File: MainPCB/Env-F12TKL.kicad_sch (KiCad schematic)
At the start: 223 parts, among them J1 TSA343G00-250J2, U1 SOT-23-5 5.5V 3.3V 500mA, U2 RP2040, Y1 3225_4P

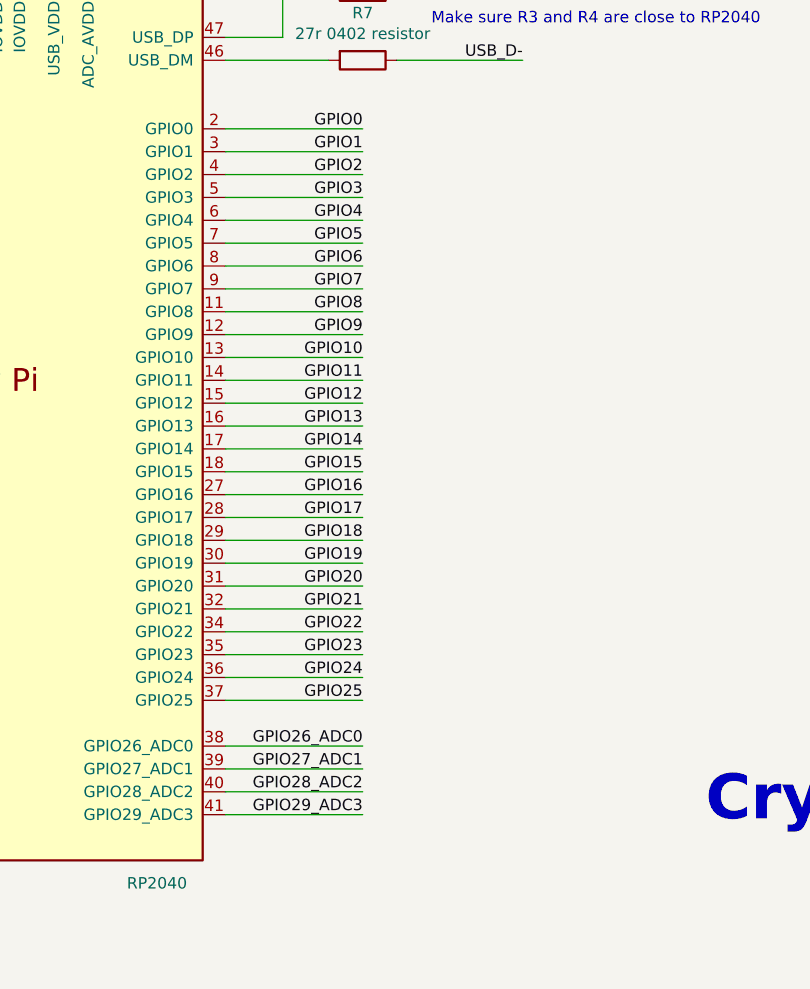
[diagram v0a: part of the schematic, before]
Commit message: wired up a whole bunch of matrix traces, now just need to add some I2C headers and some RGB connectors and some hidden cats among other illicit things like memes.
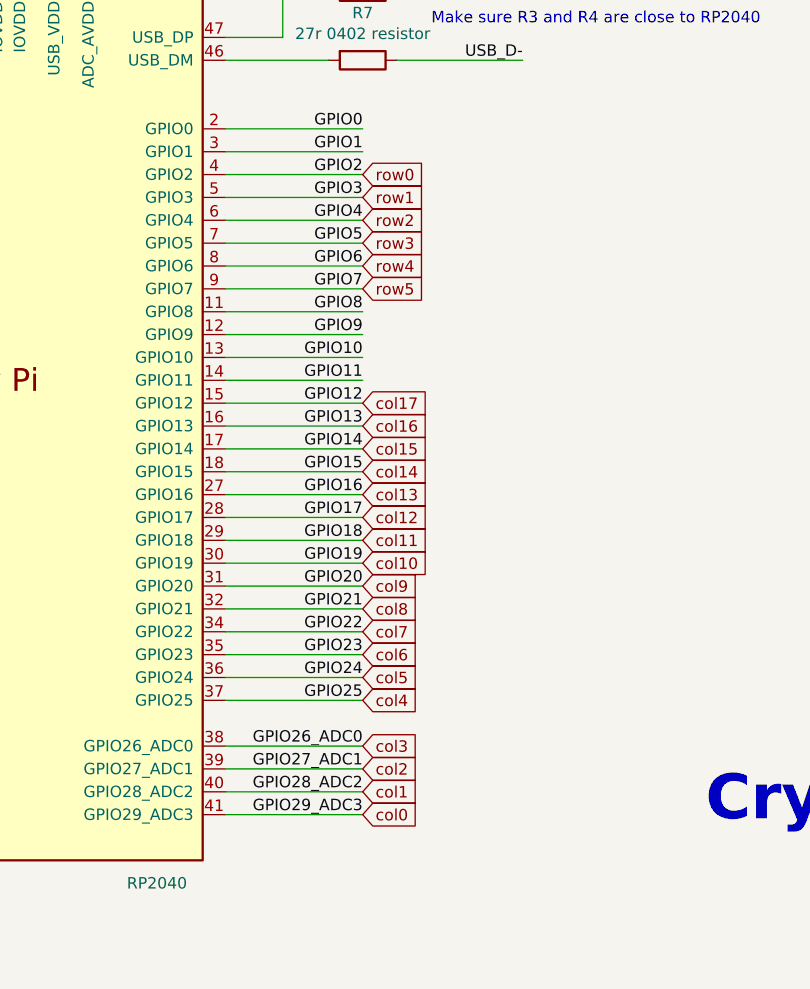
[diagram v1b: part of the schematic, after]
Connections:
- net GPIO12 is gone; now on net col17: U2.15 (GPIO12)
- net GPIO13 is gone; now on net col16: U2.16 (GPIO13)
- net GPIO14 is gone; now on net col15: U2.17 (GPIO14)
- net GPIO15 is gone; now on net col14: U2.18 (GPIO15)
- net GPIO16 is gone; now on net col13: U2.27 (GPIO16)
- net GPIO17 is gone; now on net col12: U2.28 (GPIO17)
- net GPIO18 is gone; now on net col11: U2.29 (GPIO18)
- net GPIO19 is gone; now on net col10: U2.30 (GPIO19)
- net GPIO2 is gone; now on net row0: U2.4 (GPIO2)
- net GPIO20 is gone; now on net col9: U2.31 (GPIO20)
- net GPIO21 is gone; now on net col8: U2.32 (GPIO21)
- net GPIO22 is gone; now on net col7: U2.34 (GPIO22)
- net GPIO23 is gone; now on net col6: U2.35 (GPIO23)
- net GPIO24 is gone; now on net col5: U2.36 (GPIO24)
- net GPIO25 is gone; now on net col4: U2.37 (GPIO25)
- net GPIO26_ADC0 is gone; now on net col3: U2.38 (GPIO26_ADC0)
- net GPIO27_ADC1 is gone; now on net col2: U2.39 (GPIO27_ADC1)
- net GPIO28_ADC2 is gone; now on net col1: U2.40 (GPIO28_ADC2)
- net GPIO29_ADC3 is gone; now on net col0: U2.41 (GPIO29_ADC3)
- net GPIO3 is gone; now on net row1: U2.5 (GPIO3)
- net GPIO4 is gone; now on net row2: U2.6 (GPIO4)
- net GPIO5 is gone; now on net row3: U2.7 (GPIO5)
- net GPIO6 is gone; now on net row4: U2.8 (GPIO6)
- net GPIO7 is gone; now on net row5: U2.9 (GPIO7)
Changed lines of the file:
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@@
     (effects (font (size 1.27 1.27)) (justify right bottom))
   )
+  (global_label "col0" (shape input) (at 299.72 375.92 0) (fields_autoplaced)
+    (effects (font (size 1.27 1.27)) (justify left))
+    (property "Intersheet References" "${INTERSHEET_REFS}" (id 0) (at 306.436 375.8406 0)
+      (effects (font (size 1.27 1.27)) (justify left) hide)
+    )
+  )
   (global_label "row0" (shape input) (at 31.75 43.18 180) (fields_autoplaced)
     (effects (font (size 1.27 1.27)) (justify right))
@@
     (property "Intersheet References" "${INTERSHEET_REFS}" (id 0) (at 3.81 7.62 0)
       (effects (font (size 1.27 1.27)) hide)
+    )
+  )
+  (global_label "col7" (shape input) (at 299.72 355.6 0) (fields_autoplaced)
+    (effects (font (size 1.27 1.27)) (justify left))
+    (property "Intersheet References" "${INTERSHEET_REFS}" (id 0) (at 306.436 355.5206 0)
+      (effects (font (size 1.27 1.27)) (justify left) hide)
     )
   )
@@
     )
   )
+  (global_label "col14" (shape input) (at 299.72 337.82 0) (fields_autoplaced)
+    (effects (font (size 1.27 1.27)) (justify left))
+    (property "Intersheet References" "${INTERSHEET_REFS}" (id 0) (at 306.436 337.7406 0)
+      (effects (font (size 1.27 1.27)) (justify left) hide)
+    )
+  )
   (global_label "col14" (shape input) (at 405.13 24.13 180) (fields_autoplaced)
     (effects (font (size 1.27 1.27)) (justify right))
@@
     (property "Intersheet References" "${INTERSHEET_REFS}" (id 0) (at 3.81 7.62 0)
       (effects (font (size 1.27 1.27)) hide)
+    )
+  )
+  (global_label "row4" (shape input) (at 299.72 314.96 0) (fields_autoplaced)
+    (effects (font (size 1.27 1.27)) (justify left))
+    (property "Intersheet References" "${INTERSHEET_REFS}" (id 0) (at 306.7988 314.8806 0)
+      (effects (font (size 1.27 1.27)) (justify left) hide)
+    )
+  )
+  (global_label "col17" (shape input) (at 299.72 330.2 0) (fields_autoplaced)
+    (effects (font (size 1.27 1.27)) (justify left))
+    (property "Intersheet References" "${INTERSHEET_REFS}" (id 0) (at 306.436 330.1206 0)
+      (effects (font (size 1.27 1.27)) (justify left) hide)
     )
   )
@@
     )
   )
+  (global_label "col6" (shape input) (at 299.72 358.14 0) (fields_autoplaced)
+    (effects (font (size 1.27 1.27)) (justify left))
+    (property "Intersheet References" "${INTERSHEET_REFS}" (id 0) (at 306.436 358.0606 0)
+      (effects (font (size 1.27 1.27)) (justify left) hide)
+    )
+  )
+  (global_label "col2" (shape input) (at 299.72 370.84 0) (fields_autoplaced)
+    (effects (font (size 1.27 1.27)) (justify left))
+    (property "Intersheet References" "${INTERSHEET_REFS}" (id 0) (at 306.436 370.7606 0)
+      (effects (font (size 1.27 1.27)) (justify left) hide)
+    )
+  )
+  (global_label "col9" (shape input) (at 299.72 350.52 0) (fields_autoplaced)
+    (effects (font (size 1.27 1.27)) (justify left))
+    (property "Intersheet References" "${INTERSHEET_REFS}" (id 0) (at 306.436 350.4406 0)
+      (effects (font (size 1.27 1.27)) (justify left) hide)
+    )
+  )
+  (global_label "col10" (shape input) (at 299.72 347.98 0) (fields_autoplaced)
+    (effects (font (size 1.27 1.27)) (justify left))
+    (property "Intersheet References" "${INTERSHEET_REFS}" (id 0) (at 306.436 347.9006 0)
+      (effects (font (size 1.27 1.27)) (justify left) hide)
+    )
+  )
   (global_label "col17" (shape input) (at 481.33 24.13 180) (fields_autoplaced)
     (effects (font (size 1.27 1.27)) (justify right))
@@
     (property "Intersheet References" "${INTERSHEET_REFS}" (id 0) (at 3.81 7.62 0)
       (effects (font (size 1.27 1.27)) hide)
+    )
+  )
+  (global_label "col4" (shape input) (at 299.72 363.22 0) (fields_autoplaced)
+    (effects (font (size 1.27 1.27)) (justify left))
+    (property "Intersheet References" "${INTERSHEET_REFS}" (id 0) (at 306.436 363.1406 0)
+      (effects (font (size 1.27 1.27)) (justify left) hide)
+    )
+  )
+  (global_label "col15" (shape input) (at 299.72 335.28 0) (fields_autoplaced)
+    (effects (font (size 1.27 1.27)) (justify left))
+    (property "Intersheet References" "${INTERSHEET_REFS}" (id 0) (at 306.436 335.2006 0)
+      (effects (font (size 1.27 1.27)) (justify left) hide)
     )
   )
@@
     )
   )
+  (global_label "col3" (shape input) (at 299.72 368.3 0) (fields_autoplaced)
+    (effects (font (size 1.27 1.27)) (justify left))
+    (property "Intersheet References" "${INTERSHEET_REFS}" (id 0) (at 306.436 368.2206 0)
+      (effects (font (size 1.27 1.27)) (justify left) hide)
+    )
+  )
   (global_label "col9" (shape input) (at 278.13 24.13 180) (fields_autoplaced)
     (effects (font (size 1.27 1.27)) (justify right))
@@
     )
   )
+  (global_label "row0" (shape input) (at 299.72 304.8 0) (fields_autoplaced)
+    (effects (font (size 1.27 1.27)) (justify left))
+    (property "Intersheet References" "${INTERSHEET_REFS}" (id 0) (at 322.58 340.36 0)
+      (effects (font (size 1.27 1.27)) hide)
+    )
+  )
+  (global_label "row3" (shape input) (at 299.72 312.42 0) (fields_autoplaced)
+    (effects (font (size 1.27 1.27)) (justify left))
+    (property "Intersheet References" "${INTERSHEET_REFS}" (id 0) (at 306.7988 312.3406 0)
+      (effects (font (size 1.27 1.27)) (justify left) hide)
+    )
+  )
   (global_label "col15" (shape input) (at 430.53 24.13 180) (fields_autoplaced)
     (effects (font (size 1.27 1.27)) (justify right))
@@
     )
   )
+  (global_label "col5" (shape input) (at 299.72 360.68 0) (fields_autoplaced)
+    (effects (font (size 1.27 1.27)) (justify left))
+    (property "Intersheet References" "${INTERSHEET_REFS}" (id 0) (at 306.436 360.6006 0)
+      (effects (font (size 1.27 1.27)) (justify left) hide)
+    )
+  )
+  (global_label "row1" (shape input) (at 299.72 307.34 0) (fields_autoplaced)
+    (effects (font (size 1.27 1.27)) (justify left))
+    (property "Intersheet References" "${INTERSHEET_REFS}" (id 0) (at 306.7988 307.2606 0)
+      (effects (font (size 1.27 1.27)) (justify left) hide)
+    )
+  )
+  (global_label "col11" (shape input) (at 299.72 345.44 0) (fields_autoplaced)
+    (effects (font (size 1.27 1.27)) (justify left))
+    (property "Intersheet References" "${INTERSHEET_REFS}" (id 0) (at 306.436 345.3606 0)
+      (effects (font (size 1.27 1.27)) (justify left) hide)
+    )
+  )
   (global_label "col1" (shape input) (at 74.93 24.13 180) (fields_autoplaced)
     (effects (font (size 1.27 1.27)) (justify right))
@@
     )
   )
+  (global_label "row2" (shape input) (at 299.72 309.88 0) (fields_autoplaced)
+    (effects (font (size 1.27 1.27)) (justify left))
+    (property "Intersheet References" "${INTERSHEET_REFS}" (id 0) (at 306.7988 309.8006 0)
+      (effects (font (size 1.27 1.27)) (justify left) hide)
+    )
+  )
   (global_label "row3" (shape input) (at 31.75 119.38 180) (fields_autoplaced)
     (effects (font (size 1.27 1.27)) (justify right))
@@
     )
   )
+  (global_label "col16" (shape input) (at 299.72 332.74 0) (fields_autoplaced)
+    (effects (font (size 1.27 1.27)) (justify left))
+    (property "Intersheet References" "${INTERSHEET_REFS}" (id 0) (at 306.436 332.6606 0)
+      (effects (font (size 1.27 1.27)) (justify left) hide)
+    )
+  )
   (global_label "XOUT" (shape input) (at 219.71 340.36 180) (fields_autoplaced)
     (effects (font (size 1.27 1.27)) (justify right))
@@
     )
   )
+  (global_label "col12" (shape input) (at 299.72 342.9 0) (fields_autoplaced)
+    (effects (font (size 1.27 1.27)) (justify left))
+    (property "Intersheet References" "${INTERSHEET_REFS}" (id 0) (at 306.436 342.8206 0)
+      (effects (font (size 1.27 1.27)) (justify left) hide)
+    )
+  )
   (global_label "col0" (shape input) (at 49.53 24.13 180) (fields_autoplaced)
     (effects (font (size 1.27 1.27)) (justify right))
@@
     )
   )
+  (global_label "col8" (shape input) (at 299.72 353.06 0) (fields_autoplaced)
+    (effects (font (size 1.27 1.27)) (justify left))
+    (property "Intersheet References" "${INTERSHEET_REFS}" (id 0) (at 306.436 352.9806 0)
+      (effects (font (size 1.27 1.27)) (justify left) hide)
+    )
+  )
+  (global_label "row5" (shape input) (at 299.72 317.5 0) (fields_autoplaced)
+    (effects (font (size 1.27 1.27)) (justify left))
+    (property "Intersheet References" "${INTERSHEET_REFS}" (id 0) (at 306.7988 317.4206 0)
+      (effects (font (size 1.27 1.27)) (justify left) hide)
+    )
+  )
+  (global_label "col13" (shape input) (at 299.72 340.36 0) (fields_autoplaced)
+    (effects (font (size 1.27 1.27)) (justify left))
+    (property "Intersheet References" "${INTERSHEET_REFS}" (id 0) (at 306.436 340.2806 0)
+      (effects (font (size 1.27 1.27)) (justify left) hide)
+    )
+  )
+  (global_label "col1" (shape input) (at 299.72 373.38 0) (fields_autoplaced)
+    (effects (font (size 1.27 1.27)) (justify left))
+    (property "Intersheet References" "${INTERSHEET_REFS}" (id 0) (at 306.436 373.3006 0)
+      (effects (font (size 1.27 1.27)) (justify left) hide)
+    )
+  )

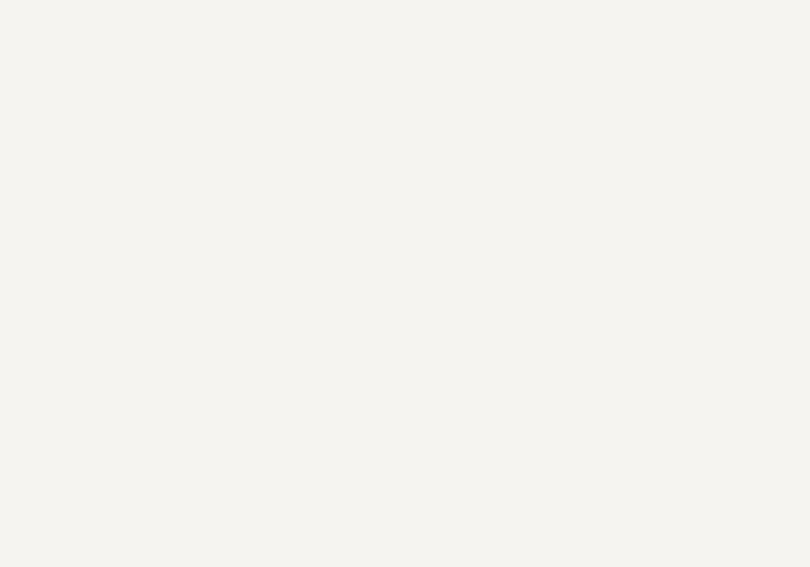
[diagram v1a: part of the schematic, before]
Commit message: added a GPIO breakout
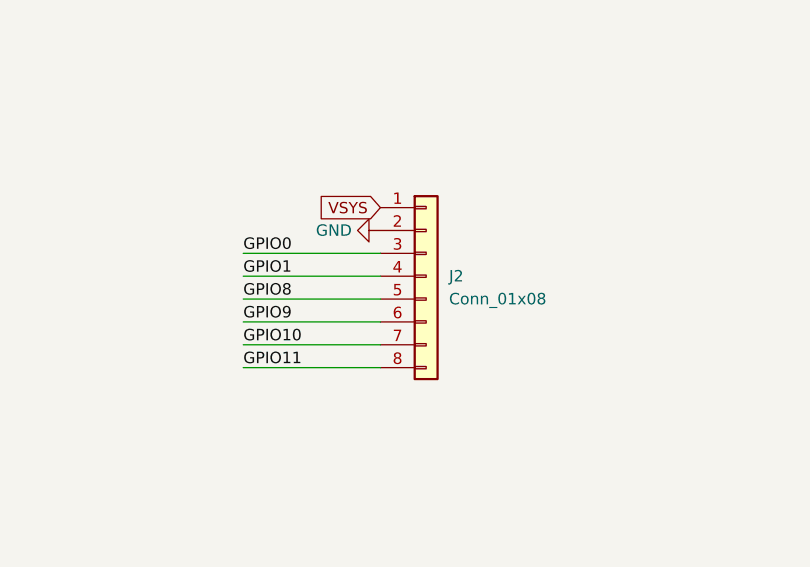
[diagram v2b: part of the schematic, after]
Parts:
- added J2: Conn_01x08, Connector_PinHeader_2.54mm:PinHeader_1x08_P2.54mm_Vertical, symbol Connector_Generic:Conn_01x08
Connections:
- net GND: now also J2.2 (Pin_2)
- net GPIO0: now also J2.3 (Pin_3)
- net GPIO1: now also J2.4 (Pin_4)
- net GPIO10: now also J2.7 (Pin_7)
- net GPIO11: now also J2.8 (Pin_8)
- net GPIO8: now also J2.5 (Pin_5)
- net GPIO9: now also J2.6 (Pin_6)
- net VBUS: now also J2.1 (Pin_1)
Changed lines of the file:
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@@
     (stroke (width 0) (type default) (color 0 0 0 0))
   )
+  (wire (pts (xy 427.99 223.52) (xy 412.75 223.52))
+    (stroke (width 0) (type default) (color 0 0 0 0))
+  )
   (wire (pts (xy 240.03 281.94) (xy 240.03 269.24))
     (stroke (width 0) (type default) (color 0 0 0 0))
@@
     (stroke (width 0) (type default) (color 0 0 0 0))
   )
+  (wire (pts (xy 427.99 231.14) (xy 412.75 231.14))
+    (stroke (width 0) (type default) (color 0 0 0 0))
+  )
   (wire (pts (xy 269.24 264.16) (xy 278.13 264.16))
     (stroke (width 0) (type default) (color 0 0 0 0))
@@
     (stroke (width 0) (type solid) (color 0 0 0 0))
   )
+  (wire (pts (xy 427.99 236.22) (xy 412.75 236.22))
+    (stroke (width 0) (type default) (color 0 0 0 0))
+  )
   (wire (pts (xy 48.26 214.63) (xy 52.07 214.63))
     (stroke (width 0) (type solid) (color 0 0 0 0))
@@
     (stroke (width 0) (type default) (color 0 0 0 0))
   )
+  (wire (pts (xy 427.99 228.6) (xy 412.75 228.6))
+    (stroke (width 0) (type default) (color 0 0 0 0))
+  )
   (wire (pts (xy 284.48 325.12) (xy 299.72 325.12))
     (stroke (width 0) (type default) (color 0 0 0 0))
@@
     (stroke (width 0) (type default) (color 0 0 0 0))
   )
+  (wire (pts (xy 427.99 233.68) (xy 412.75 233.68))
+    (stroke (width 0) (type default) (color 0 0 0 0))
+  )
   (wire (pts (xy 311.15 257.81) (xy 311.15 260.35))
     (stroke (width 0) (type default) (color 0 0 0 0))
@@
     (stroke (width 0) (type default) (color 0 0 0 0))
   )
+  (wire (pts (xy 427.99 226.06) (xy 412.75 226.06))
+    (stroke (width 0) (type default) (color 0 0 0 0))
+  )
   (wire (pts (xy 300.99 250.19) (xy 300.99 248.92))
     (stroke (width 0) (type default) (color 0 0 0 0))
@@
     (effects (font (size 1.27 1.27)) (justify right bottom))
   )
+  (label "GPIO1" (at 412.75 226.06 0)
+    (effects (font (size 1.27 1.27)) (justify left bottom))
+  )
   (label "GPIO9" (at 299.72 322.58 180)
     (effects (font (size 1.27 1.27)) (justify right bottom))
@@
     (effects (font (size 1.27 1.27)) (justify right bottom))
   )
+  (label "GPIO8" (at 412.75 228.6 0)
+    (effects (font (size 1.27 1.27)) (justify left bottom))
+  )
   (label "GPIO5" (at 299.72 312.42 180)
     (effects (font (size 1.27 1.27)) (justify right bottom))
@@
     (effects (font (size 1.27 1.27)) (justify right bottom))
   )
+  (label "GPIO9" (at 412.75 231.14 0)
+    (effects (font (size 1.27 1.27)) (justify left bottom))
+  )
   (label "QSPI_SD1" (at 60.96 339.09 0)
     (effects (font (size 1.27 1.27)) (justify left bottom))
@@
     (effects (font (size 1.27 1.27)) (justify right bottom))
   )
+  (label "GPIO0" (at 412.75 223.52 0)
+    (effects (font (size 1.27 1.27)) (justify left bottom))
+  )
   (label "QSPI_SD0" (at 60.96 336.55 0)
     (effects (font (size 1.27 1.27)) (justify left bottom))
@@
     (effects (font (size 1.27 1.27)) (justify left bottom))
   )
+  (label "GPIO11" (at 412.75 236.22 0)
+    (effects (font (size 1.27 1.27)) (justify left bottom))
+  )
   (label "QSPI_SS" (at 62.23 328.93 0)
     (effects (font (size 1.27 1.27)) (justify left bottom))
@@
     (effects (font (size 1.27 1.27)) (justify right bottom))
   )
+  (label "GPIO10" (at 412.75 233.68 0)
+    (effects (font (size 1.27 1.27)) (justify left bottom))
+  )
   (label "GPIO8" (at 299.72 320.04 180)
     (effects (font (size 1.27 1.27)) (justify right bottom))
@@
     )
   )
+  (global_label "VSYS" (shape input) (at 427.99 218.44 180) (fields_autoplaced)
+    (effects (font (size 1.25 1.25)) (justify right))
+    (property "Intersheet References" "${INTERSHEET_REFS}" (id 0) (at 420.9036 218.3619 0)
+      (effects (font (size 1.25 1.25)) (justify right) hide)
+    )
+  )
   (global_label "VSYS" (shape input) (at 55.88 256.54 180) (fields_autoplaced)
     (effects (font (size 0.508 0.508)) (justify right))
@@
     (pin "2")
   )
+  (symbol (lib_id "Connector_Generic:Conn_01x08") (at 433.07 226.06 0) (unit 1)
+    (in_bom yes) (on_board yes) (fields_autoplaced)
+    (property "Reference" "J2" (id 0) (at 435.61 226.0599 0)
+      (effects (font (size 1.27 1.27)) (justify left))
+    )
+    (property "Value" "Conn_01x08" (id 1) (at 435.61 228.5999 0)
+      (effects (font (size 1.27 1.27)) (justify left))
+    )
+    (property "Footprint" "Connector_PinHeader_2.54mm:PinHeader_1x08_P2.54mm_Vertical" (id 2) (at 433.07 226.06 0)
+      (effects (font (size 1.27 1.27)) hide)
+    )
+    (property "Datasheet" "~" (id 3) (at 433.07 226.06 0)
+      (effects (font (size 1.27 1.27)) hide)
+    )
+    (pin "1")
+    (pin "2")
+    (pin "3")
+    (pin "4")
+    (pin "5")
+    (pin "6")
+    (pin "7")
+    (pin "8")
+  )
   (symbol (lib_id "Mechanical:MountingHole") (at 140.97 204.47 0) (unit 1)
     (in_bom yes) (on_board yes) (fields_autoplaced)
@@
     )
   )
+  (symbol (lib_id "power:GND") (at 427.99 220.98 270) (unit 1)
+    (in_bom yes) (on_board yes) (fields_autoplaced)
+    (property "Reference" "#PWR0129" (id 0) (at 421.64 220.98 0)
+      (effects (font (size 1.27 1.27)) hide)
+    )
+    (property "Value" "GND" (id 1) (at 424.815 220.9799 90)
+      (effects (font (size 1.27 1.27)) (justify right))
+    )
+    (property "Footprint" "" (id 2) (at 427.99 220.98 0)
+      (effects (font (size 1.27 1.27)) hide)
+    )
+    (property "Datasheet" "" (id 3) (at 427.99 220.98 0)
+      (effects (font (size 1.27 1.27)) hide)
+    )
+    (pin "1")
+  )
   (symbol (lib_id "Device:C") (at 311.15 254 0) (unit 1)
     (in_bom yes) (on_board yes)
@@
       (reference "#PWR0127") (unit 1) (value "GND") (footprint "")
     )
+    (path "/7e1e49e9-f4d0-4bca-adfe-0e1738f4fba2"
+      (reference "#PWR0129") (unit 1) (value "GND") (footprint "")
+    )
     (path "/982ef67d-acb9-4099-8988-180bea760833"
       (reference "C1") (unit 1) (value "10uf 0402") (footprint "Capacitor_SMD:C_0402_1005Metric")
@@
       (reference "J1") (unit 1) (value "TSA343G00-250J2") (footprint "Button_Switch_SMD:SW_Push_SPST_NO_Alps_SKRK")
     )
+    (path "/6b964c87-5d27-4e6a-a44b-bb3ef2030658"
+      (reference "J2") (unit 1) (value "Conn_01x08") (footprint "Connector_PinHeader_2.54mm:PinHeader_1x08_P2.54mm_Vertical")
+    )
     (path "/c6935672-69a4-4ca5-95eb-adb7825d0094"
